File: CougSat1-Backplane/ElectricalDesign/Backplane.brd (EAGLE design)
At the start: 92 x 85 mm, 16 parts, among them J1 COUGSATBUSBACKPLANE, J2 COUGSATBUSBACKPLANE, J3 COUGSATBUSBACKPLANE, J4 COUGSATBUSBACKPLANE, J5 COUGSATBUSBACKPLANE, J6 COUGSATBUSBACKPLANE, J7 COUGSATBUSBACKPLANE, J8 COUGSATBUSBACKPLANE

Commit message: Updated Backplane Schematic
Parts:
- removed H3, H4: (no value), CougsInSpace:HOLE-3.3MM_PLAIN
- removed IMG1: COUGSINSPACELOGOSMALL, CougsInSpace:COUGSINSPACELOGO_SMALL
- removed IMG2: COUGSINSPACELOGOTEXT, CougsInSpace:COUGSINSPACETEXT
- removed IMG3: SIGNATUREHENDRIK, CougsInSpace:SIGNATURE_HENDRIK-MONOGRAM
- removed IMG4: SIGNATUREHENDRIK-HAM, CougsInSpace:SIGNATURE_HENDRIK-HAM
- added C1, C2: 100nF 10%, CougsInSpace-Capacitors:1608
- added J10, J9: Deployment Switch, CougsInSpace-Connectors:PICOLOCK1.5-04
- added R1, R2: 0Ω <20mΩ, CougsInSpace-Resistors:1608
- H1, H2: value (none) -> M3; device CougsInSpace:HOLE-3.3MM_PLAIN -> CougsInSpace-Hardware:MOUNTING_HOLE-3.3
- J1, J2, J3, J4, J5, J6, J7, J8: value COUGSATBUSBACKPLANE -> CougSat Socket; device CougsInSpace:COUGSATBUS_FEMALE-SODIMM -> CougsInSpace-Connectors:SODIMM-DDR1
- moved H2 75.1 mm to (14.0, 0.00)
- moved J1 62.6 mm to (0.00, -37.5)
- moved J2 62.6 mm to (0.00, -28.5)
- moved J3 62.6 mm to (0.00, -19.5)
- moved J4 62.6 mm to (0.00, -10.5)
- moved J5 62.6 mm to (0.00, 10.5)
- moved J6 62.6 mm to (0.00, 19.5)
- moved J7 62.6 mm to (0.00, 28.5)
- moved J8 62.6 mm to (0.00, 37.5)
- moved H1 17.3 mm to (-14.0, 0.00)
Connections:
- removed net COM_IRQ: J1.154, J1.156, J2.154, J2.156, J3.154, J3.156, J4.154, J4.156, J5.154, J5.156, J6.154, J6.156, J7.154, J7.156, J8.154, J8.156
- removed net COM_USART_CLK: J1.150, J1.152, J2.150, J2.152, J3.150, J3.152, J4.150, J4.152, J5.150, J5.152, J6.150, J6.152, J7.150, J7.152, J8.150, J8.152
- removed net COM_USART_RX: J1.146, J1.148, J2.146, J2.148, J3.146, J3.148, J4.146, J4.148, J5.146, J5.148, J6.146, J6.148, J7.146, J7.148, J8.146, J8.148
- removed net COM_USART_TX: J1.142, J1.144, J2.142, J2.144, J3.142, J3.144, J4.142, J4.144, J5.142, J5.144, J6.142, J6.144, J7.142, J7.144, J8.142, J8.144
- removed net CTRL_RESET: J1.174, J1.176, J2.174, J2.176, J3.174, J3.176, J4.174, J4.176, J5.174, J5.176, J6.174, J6.176, J7.174, J7.176, J8.174, J8.176
- removed net GPIO_153: J1.153, J2.153, J3.153, J4.153, J5.153, J6.153, J7.153, J8.153
- removed net GPIO_155: J1.155, J2.155, J3.155, J4.155, J5.155, J6.155, J7.155, J8.155
- removed net GPIO_157: J1.157, J2.157, J3.157, J4.157, J5.157, J6.157, J7.157, J8.157
- removed net GPIO_158: J1.158, J2.158, J3.158, J4.158, J5.158, J6.158, J7.158, J8.158
- removed net GPIO_159: J1.159, J2.159, J3.159, J4.159, J5.159, J6.159, J7.159, J8.159
- removed net GPIO_161: J1.161, J2.161, J3.161, J4.161, J5.161, J6.161, J7.161, J8.161
- removed net GPIO_163: J1.163, J2.163, J3.163, J4.163, J5.163, J6.163, J7.163, J8.163
- removed net GPIO_165: J1.165, J2.165, J3.165, J4.165, J5.165, J6.165, J7.165, J8.165
- removed net GPIO_167: J1.167, J2.167, J3.167, J4.167, J5.167, J6.167, J7.167, J8.167
- removed net PMIC_I2C_SCL: J1.183, J2.183, J3.183, J4.183, J5.183, J6.183, J7.183, J8.183
- removed net PMIC_I2C_SDA: J1.181, J2.181, J3.181, J4.181, J5.181, J6.181, J7.181, J8.181
- removed net PWR_CTRL_UMB: J1.170, J1.172, J2.170, J2.172, J3.170, J3.172, J4.170, J4.172, J5.170, J5.172, J6.170, J6.172, J7.170, J7.172, J8.170, J8.172
- removed net SUP_3V3_0: J1.10, J1.2, J1.4, J1.6, J1.8, J2.10, J2.2, J2.4, J2.6, J2.8, J3.10, J3.2, J3.4, J3.6, J3.8, J4.10, J4.2, J4.4, J4.6, J4.8, J5.10, J5.2, J5.4, J5.6, J5.8, J6.10, J6.2, J6.4, J6.6, J6.8, J7.10, J7.2, J7.4, J7.6, J7.8, J8.10, J8.2, J8.4, J8.6, J8.8
- removed net SUP_3V3_1: J1.12, J1.14, J1.16, J1.18, J1.20, J2.12, J2.14, J2.16, J2.18, J2.20, J3.12, J3.14, J3.16, J3.18, J3.20, J4.12, J4.14, J4.16, J4.18, J4.20, J5.12, J5.14, J5.16, J5.18, J5.20, J6.12, J6.14, J6.16, J6.18, J6.20, J7.12, J7.14, J7.16, J7.18, J7.20, J8.12, J8.14, J8.16, J8.18, J8.20
- removed net SUP_3V3_2: J1.21, J1.23, J1.25, J1.27, J1.29, J1.31, J1.33, J1.35, J1.37, J1.39, J2.21, J2.23, J2.25, J2.27, J2.29, J2.31, J2.33, J2.35, J2.37, J2.39, J3.21, J3.23, J3.25, J3.27, J3.29, J3.31, J3.33, J3.35, J3.37, J3.39, J4.21, J4.23, J4.25, J4.27, J4.29, J4.31, J4.33, J4.35, J4.37, J4.39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
- removed net SUP_3V3_3: J1.22, J1.24, J1.26, J1.28, J1.30, J1.32, J1.34, J1.36, J1.38, J1.40, J2.22, J2.24, J2.26, J2.28, J2.30, J2.32, J2.34, J2.36, J2.38, J2.40, J3.22, J3.24, J3.26, J3.28, J3.30, J3.32, J3.34, J3.36, J3.38, J3.40, J4.22, J4.24, J4.26, J4.28, J4.30, J4.32, J4.34, J4.36, J4.38, J4.40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
- removed net SUP_3V3_4: J1.42, J1.44, J1.46, J1.48, J1.50, J2.42, J2.44, J2.46, J2.48, J2.50, J3.42, J3.44, J3.46, J3.48, J3.50, J4.42, J4.44, J4.46, J4.48, J4.50, J5.42, J5.44, J5.46, J5.48, J5.50, J6.42, J6.44, J6.46, J6.48, J6.50, J7.42, J7.44, J7.46, J7.48, J7.50, J8.42, J8.44, J8.46, J8.48, J8.50
- removed net SUP_3V3_5: J1.52, J1.54, J1.56, J1.58, J1.60, J2.52, J2.54, J2.56, J2.58, J2.60, J3.52, J3.54, J3.56, J3.58, J3.60, J4.52, J4.54, J4.56, J4.58, J4.60, J5.52, J5.54, J5.56, J5.58, J5.60, J6.52, J6.54, J6.56, J6.58, J6.60, J7.52, J7.54, J7.56, J7.58, J7.60, J8.52, J8.54, J8.56, J8.58, J8.60
- removed net SUP_5V0_0: J1.62, J1.64, J1.66, J1.68, J1.70, J1.72, J1.74, J1.76, J1.78, J1.80, J2.62, J2.64, J2.66, J2.68, J2.70, J2.72, J2.74, J2.76, J2.78, J2.80, J3.62, J3.64, J3.66, J3.68, J3.70, J3.72, J3.74, J3.76, J3.78, J3.80, J4.62, J4.64, J4.66, J4.68, J4.70, J4.72, J4.74, J4.76, J4.78, J4.80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
- removed net SUP_5V0_1: J1.71, J1.73, J1.75, J1.77, J1.79, J1.81, J1.83, J1.85, J1.87, J1.89, J2.71, J2.73, J2.75, J2.77, J2.79, J2.81, J2.83, J2.85, J2.87, J2.89, J3.71, J3.73, J3.75, J3.77, J3.79, J3.81, J3.83, J3.85, J3.87, J3.89, J4.71, J4.73, J4.75, J4.77, J4.79, J4.81, J4.83, J4.85, J4.87, J4.89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
- removed net SUP_5VIN: J1.182, J1.184, J1.186, J1.188, J1.190, J1.192, J1.194, J1.196, J1.198, J1.200, J2.182, J2.184, J2.186, J2.188, J2.190, J2.192, J2.194, J2.196, J2.198, J2.200, J3.182, J3.184, J3.186, J3.188, J3.190, J3.192, J3.194, J3.196, J3.198, J3.200, J4.182, J4.184, J4.186, J4.188, J4.190, J4.192, J4.194, J4.196, J4.198, J4.200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
- removed net SUP_UNREG_0: J1.101, J1.103, J1.105, J1.107, J1.109, J1.91, J1.93, J1.95, J1.97, J1.99, J2.101, J2.103, J2.105, J2.107, J2.109, J2.91, J2.93, J2.95, J2.97, J2.99, J3.101, J3.103, J3.105, J3.107, J3.109, J3.91, J3.93, J3.95, J3.97, J3.99, J4.101, J4.103, J4.105, J4.107, J4.109, J4.91, J4.93, J4.95, J4.97, J4.99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
- removed net SUP_UNREG_1: J1.111, J1.113, J1.115, J1.117, J1.119, J1.121, J1.123, J1.125, J1.127, J1.129, J2.111, J2.113, J2.115, J2.117, J2.119, J2.121, J2.123, J2.125, J2.127, J2.129, J3.111, J3.113, J3.115, J3.117, J3.119, J3.121, J3.123, J3.125, J3.127, J3.129, J4.111, J4.113, J4.115, J4.117, J4.119, J4.121, J4.123, J4.125, J4.127, J4.129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
- new net BUS_JTAG_EN-0: J1.186, J1.188, J2.186, J2.188, J3.186, J3.188, J4.186, J4.188, J5.186, J5.188, J6.186, J6.188, J7.186, J7.188, J8.186, J8.188
- new net BUS_JTAG_EN-1: J1.190, J1.192, J2.190, J2.192, J3.190, J3.192, J4.190, J4.192, J5.190, J5.192, J6.190, J6.192, J7.190, J7.192, J8.190, J8.192
- new net BUS_JTAG_EN-2: J1.194, J1.196, J2.194, J2.196, J3.194, J3.196, J4.194, J4.196, J5.194, J5.196, J6.194, J6.196, J7.194, J7.196, J8.194, J8.196
- new net BUS_JTAG_EN-3: J1.198, J1.200, J2.198, J2.200, J3.198, J3.200, J4.198, J4.200, J5.198, J5.200, J6.198, J6.200, J7.198, J7.200, J8.198, J8.200
- new net CHASSIS: C1.1, C2.1, H1.1, H1.V1, H1.V2, H1.V3, H1.V4, H1.V5, H1.V6, H1.V7, H1.V8, H2.1, H2.V1, H2.V2, H2.V3, H2.V4, H2.V5, H2.V6, H2.V7, H2.V8, R1.2, R2.2
- new net COM_SPI_CS: J1.145, J1.147, J2.145, J2.147, J3.145, J3.147, J4.145, J4.147, J5.145, J5.147, J6.145, J6.147, J7.145, J7.147, J8.145, J8.147
- new net COM_SPI_MISO: J1.137, J1.139, J2.137, J2.139, J3.137, J3.139, J4.137, J4.139, J5.137, J5.139, J6.137, J6.139, J7.137, J7.139, J8.137, J8.139
- new net COM_SPI_MOSI: J1.141, J1.143, J2.141, J2.143, J3.141, J3.143, J4.141, J4.143, J5.141, J5.143, J6.141, J6.143, J7.141, J7.143, J8.141, J8.143
- new net COM_SPI_SCK: J1.133, J1.135, J2.133, J2.135, J3.133, J3.135, J4.133, J4.135, J5.133, J5.135, J6.133, J6.135, J7.133, J7.135, J8.133, J8.135
- new net CTRL_!RESET: J1.165, J1.167, J2.165, J2.167, J3.165, J3.167, J4.165, J4.167, J5.165, J5.167, J6.165, J6.167, J7.165, J7.167, J8.165, J8.167
- new net GPIO-0: J1.81, J1.83, J2.81, J2.83, J3.81, J3.83, J4.81, J4.83, J5.81, J5.83, J6.81, J6.83, J7.81, J7.83, J8.81, J8.83
- new net GPIO-1: J1.85, J1.87, J2.85, J2.87, J3.85, J3.87, J4.85, J4.87, J5.85, J5.87, J6.85, J6.87, J7.85, J7.87, J8.85, J8.87
- new net GPIO-2: J1.89, J1.91, J2.89, J2.91, J3.89, J3.91, J4.89, J4.91, J5.89, J5.91, J6.89, J6.91, J7.89, J7.91, J8.89, J8.91
- new net GPIO-3: J1.93, J1.95, J2.93, J2.95, J3.93, J3.95, J4.93, J4.95, J5.93, J5.95, J6.93, J6.95, J7.93, J7.95, J8.93, J8.95
- new net GPIO-4: J1.97, J1.99, J2.97, J2.99, J3.97, J3.99, J4.97, J4.99, J5.97, J5.99, J6.97, J6.99, J7.97, J7.99, J8.97, J8.99
- new net GPIO-5: J1.101, J1.103, J2.101, J2.103, J3.101, J3.103, J4.101, J4.103, J5.101, J5.103, J6.101, J6.103, J7.101, J7.103, J8.101, J8.103
- new net GPIO-6: J1.105, J1.107, J2.105, J2.107, J3.105, J3.107, J4.105, J4.107, J5.105, J5.107, J6.105, J6.107, J7.105, J7.107, J8.105, J8.107
- new net GPIO-7: J1.109, J1.111, J2.109, J2.111, J3.109, J3.111, J4.109, J4.111, J5.109, J5.111, J6.109, J6.111, J7.109, J7.111, J8.109, J8.111
- new net GPIO-8: J1.113, J1.115, J2.113, J2.115, J3.113, J3.115, J4.113, J4.115, J5.113, J5.115, J6.113, J6.115, J7.113, J7.115, J8.113, J8.115
- new net GPIO-9: J1.117, J1.119, J2.117, J2.119, J3.117, J3.119, J4.117, J4.119, J5.117, J5.119, J6.117, J6.119, J7.117, J7.119, J8.117, J8.119
- new net PR_3.3V-0: J1.1, J1.2, J1.3, J1.4, J2.1, J2.2, J2.3, J2.4, J3.1, J3.2, J3.3, J3.4, J4.1, J4.2, J4.3, J4.4, J5.1, J5.2, J5.3, J5.4, J6.1, J6.2, J6.3, J6.4, J7.1, J7.2, J7.3, J7.4, J8.1, J8.2, J8.3, J8.4
- new net PR_3.3V-1: J1.5, J1.6, J1.7, J1.8, J2.5, J2.6, J2.7, J2.8, J3.5, J3.6, J3.7, J3.8, J4.5, J4.6, J4.7, J4.8, J5.5, J5.6, J5.7, J5.8, J6.5, J6.6, J6.7, J6.8, J7.5, J7.6, J7.7, J7.8, J8.5, J8.6, J8.7, J8.8
- new net PR_3.3V-10: J1.41, J1.42, J1.43, J1.44, J2.41, J2.42, J2.43, J2.44, J3.41, J3.42, J3.43, J3.44, J4.41, J4.42, J4.43, J4.44, J5.41, J5.42, J5.43, J5.44, J6.41, J6.42, J6.43, J6.44, J7.41, J7.42, J7.43, J7.44, J8.41, J8.42, J8.43, J8.44
- new net PR_3.3V-11: J1.45, J1.46, J1.47, J1.48, J2.45, J2.46, J2.47, J2.48, J3.45, J3.46, J3.47, J3.48, J4.45, J4.46, J4.47, J4.48, J5.45, J5.46, J5.47, J5.48, J6.45, J6.46, J6.47, J6.48, J7.45, J7.46, J7.47, J7.48, J8.45, J8.46, J8.47, J8.48
- new net PR_3.3V-12: J1.49, J1.50, J1.51, J1.52, J2.49, J2.50, J2.51, J2.52, J3.49, J3.50, J3.51, J3.52, J4.49, J4.50, J4.51, J4.52, J5.49, J5.50, J5.51, J5.52, J6.49, J6.50, J6.51, J6.52, J7.49, J7.50, J7.51, J7.52, J8.49, J8.50, J8.51, J8.52
- new net PR_3.3V-2: J1.10, J1.11, J1.12, J1.9, J2.10, J2.11, J2.12, J2.9, J3.10, J3.11, J3.12, J3.9, J4.10, J4.11, J4.12, J4.9, J5.10, J5.11, J5.12, J5.9, J6.10, J6.11, J6.12, J6.9, J7.10, J7.11, J7.12, J7.9, J8.10, J8.11, J8.12, J8.9
- new net PR_3.3V-3: J1.13, J1.14, J1.15, J1.16, J2.13, J2.14, J2.15, J2.16, J3.13, J3.14, J3.15, J3.16, J4.13, J4.14, J4.15, J4.16, J5.13, J5.14, J5.15, J5.16, J6.13, J6.14, J6.15, J6.16, J7.13, J7.14, J7.15, J7.16, J8.13, J8.14, J8.15, J8.16
- new net PR_3.3V-4: J1.17, J1.18, J1.19, J1.20, J2.17, J2.18, J2.19, J2.20, J3.17, J3.18, J3.19, J3.20, J4.17, J4.18, J4.19, J4.20, J5.17, J5.18, J5.19, J5.20, J6.17, J6.18, J6.19, J6.20, J7.17, J7.18, J7.19, J7.20, J8.17, J8.18, J8.19, J8.20
- new net PR_3.3V-5: J1.21, J1.22, J1.23, J1.24, J2.21, J2.22, J2.23, J2.24, J3.21, J3.22, J3.23, J3.24, J4.21, J4.22, J4.23, J4.24, J5.21, J5.22, J5.23, J5.24, J6.21, J6.22, J6.23, J6.24, J7.21, J7.22, J7.23, J7.24, J8.21, J8.22, J8.23, J8.24
- new net PR_3.3V-6: J1.25, J1.26, J1.27, J1.28, J2.25, J2.26, J2.27, J2.28, J3.25, J3.26, J3.27, J3.28, J4.25, J4.26, J4.27, J4.28, J5.25, J5.26, J5.27, J5.28, J6.25, J6.26, J6.27, J6.28, J7.25, J7.26, J7.27, J7.28, J8.25, J8.26, J8.27, J8.28
- new net PR_3.3V-7: J1.29, J1.30, J1.31, J1.32, J2.29, J2.30, J2.31, J2.32, J3.29, J3.30, J3.31, J3.32, J4.29, J4.30, J4.31, J4.32, J5.29, J5.30, J5.31, J5.32, J6.29, J6.30, J6.31, J6.32, J7.29, J7.30, J7.31, J7.32, J8.29, J8.30, J8.31, J8.32
- new net PR_3.3V-8: J1.33, J1.34, J1.35, J1.36, J2.33, J2.34, J2.35, J2.36, J3.33, J3.34, J3.35, J3.36, J4.33, J4.34, J4.35, J4.36, J5.33, J5.34, J5.35, J5.36, J6.33, J6.34, J6.35, J6.36, J7.33, J7.34, J7.35, J7.36, J8.33, J8.34, J8.35, J8.36
- new net PR_3.3V-9: J1.37, J1.38, J1.39, J1.40, J2.37, J2.38, J2.39, J2.40, J3.37, J3.38, J3.39, J3.40, J4.37, J4.38, J4.39, J4.40, J5.37, J5.38, J5.39, J5.40, J6.37, J6.38, J6.39, J6.40, J7.37, J7.38, J7.39, J7.40, J8.37, J8.38, J8.39, J8.40
- new net PR_BATT-0: J1.53, J1.54, J1.55, J1.56, J2.53, J2.54, J2.55, J2.56, J3.53, J3.54, J3.55, J3.56, J4.53, J4.54, J4.55, J4.56, J5.53, J5.54, J5.55, J5.56, J6.53, J6.54, J6.55, J6.56, J7.53, J7.54, J7.55, J7.56, J8.53, J8.54, J8.55, J8.56
- new net PR_BATT-1: J1.57, J1.58, J1.59, J1.60, J2.57, J2.58, J2.59, J2.60, J3.57, J3.58, J3.59, J3.60, J4.57, J4.58, J4.59, J4.60, J5.57, J5.58, J5.59, J5.60, J6.57, J6.58, J6.59, J6.60, J7.57, J7.58, J7.59, J7.60, J8.57, J8.58, J8.59, J8.60
- new net PR_BATT-2: J1.61, J1.62, J1.63, J1.64, J2.61, J2.62, J2.63, J2.64, J3.61, J3.62, J3.63, J3.64, J4.61, J4.62, J4.63, J4.64, J5.61, J5.62, J5.63, J5.64, J6.61, J6.62, J6.63, J6.64, J7.61, J7.62, J7.63, J7.64, J8.61, J8.62, J8.63, J8.64
- new net PR_BATT-3: J1.65, J1.66, J1.67, J1.68, J2.65, J2.66, J2.67, J2.68, J3.65, J3.66, J3.67, J3.68, J4.65, J4.66, J4.67, J4.68, J5.65, J5.66, J5.67, J5.68, J6.65, J6.66, J6.67, J6.68, J7.65, J7.66, J7.67, J7.68, J8.65, J8.66, J8.67, J8.68
- new net PR_BATT-4: J1.69, J1.70, J1.71, J1.72, J2.69, J2.70, J2.71, J2.72, J3.69, J3.70, J3.71, J3.72, J4.69, J4.70, J4.71, J4.72, J5.69, J5.70, J5.71, J5.72, J6.69, J6.70, J6.71, J6.72, J7.69, J7.70, J7.71, J7.72, J8.69, J8.70, J8.71, J8.72
- new net PR_BATT-5: J1.73, J1.74, J1.75, J1.76, J2.73, J2.74, J2.75, J2.76, J3.73, J3.74, J3.75, J3.76, J4.73, J4.74, J4.75, J4.76, J5.73, J5.74, J5.75, J5.76, J6.73, J6.74, J6.75, J6.76, J7.73, J7.74, J7.75, J7.76, J8.73, J8.74, J8.75, J8.76
- new net PR_BATT-6: J1.77, J1.78, J1.79, J1.80, J2.77, J2.78, J2.79, J2.80, J3.77, J3.78, J3.79, J3.80, J4.77, J4.78, J4.79, J4.80, J5.77, J5.78, J5.79, J5.80, J6.77, J6.78, J6.79, J6.80, J7.77, J7.78, J7.79, J7.80, J8.77, J8.78, J8.79, J8.80
- net BUS_I2C0_IRQ: now also J1.181, J1.183, J2.181, J2.183, J3.181, J3.183, J4.181, J4.183, J5.181, J5.183, J6.181, J6.183, J7.181, J7.183, J8.181, J8.183; no longer J1.177, J1.179, J2.177, J2.179, J3.177, J3.179, J4.177, J4.179, J5.177, J5.179, J6.177, J6.179, J7.177, J7.179, J8.177, J8.179
- net BUS_I2C0_SCL: now also J1.177, J1.179, J2.177, J2.179, J3.177, J3.179, J4.177, J4.179, J5.177, J5.179, J6.177, J6.179, J7.177, J7.179, J8.177, J8.179; no longer J1.173, J1.175, J2.173, J2.175, J3.173, J3.175, J4.173, J4.175, J5.173, J5.175, J6.173, J6.175, J7.173, J7.175, J8.173, J8.175
- net BUS_I2C0_SDA: now also J1.173, J1.175, J2.173, J2.175, J3.173, J3.175, J4.173, J4.175, J5.173, J5.175, J6.173, J6.175, J7.173, J7.175, J8.173, J8.175; no longer J1.169, J1.171, J2.169, J2.171, J3.169, J3.171, J4.169, J4.171, J5.169, J5.171, J6.169, J6.171, J7.169, J7.171, J8.169, J8.171
- net BUS_I2C1_IRQ: now also J1.129, J1.131, J2.129, J2.131, J3.129, J3.131, J4.129, J4.131, J5.129, J5.131, J6.129, J6.131, J7.129, J7.131, J8.129, J8.131; no longer J1.164, J2.164, J3.164, J4.164, J5.164, J6.164, J7.164, J8.164
- net BUS_I2C1_SCL: now also J1.125, J1.127, J2.125, J2.127, J3.125, J3.127, J4.125, J4.127, J5.125, J5.127, J6.125, J6.127, J7.125, J7.127, J8.125, J8.127; no longer J1.160, J2.160, J3.160, J4.160, J5.160, J6.160, J7.160, J8.160
- net BUS_I2C1_SDA: now also J1.121, J1.123, J2.121, J2.123, J3.121, J3.123, J4.121, J4.123, J5.121, J5.123, J6.121, J6.123, J7.121, J7.123, J8.121, J8.123; no longer J1.162, J2.162, J3.162, J4.162, J5.162, J6.162, J7.162, J8.162
- net BUS_SPI_MISO: now also J1.153, J1.155, J2.153, J2.155, J3.153, J3.155, J4.153, J4.155, J5.153, J5.155, J6.153, J6.155, J7.153, J7.155, J8.153, J8.155; no longer J1.145, J1.147, J2.145, J2.147, J3.145, J3.147, J4.145, J4.147, J5.145, J5.147, J6.145, J6.147, J7.145, J7.147, J8.145, J8.147
- net BUS_SPI_MOSI: now also J1.157, J1.159, J2.157, J2.159, J3.157, J3.159, J4.157, J4.159, J5.157, J5.159, J6.157, J6.159, J7.157, J7.159, J8.157, J8.159; no longer J1.149, J1.151, J2.149, J2.151, J3.149, J3.151, J4.149, J4.151, J5.149, J5.151, J6.149, J6.151, J7.149, J7.151, J8.149, J8.151
- net BUS_SPI_SCK: now also J1.149, J1.151, J2.149, J2.151, J3.149, J3.151, J4.149, J4.151, J5.149, J5.151, J6.149, J6.151, J7.149, J7.151, J8.149, J8.151; no longer J1.141, J1.143, J2.141, J2.143, J3.141, J3.143, J4.141, J4.143, J5.141, J5.143, J6.141, J6.143, J7.141, J7.143, J8.141, J8.143
- net CTRL_SYNC: now also J1.169, J1.171, J2.169, J2.171, J3.169, J3.171, J4.169, J4.171, J5.169, J5.171, J6.169, J6.171, J7.169, J7.171, J8.169, J8.171; no longer J1.178, J1.180, J2.178, J2.180, J3.178, J3.180, J4.178, J4.180, J5.178, J5.180, J6.178, J6.180, J7.178, J7.180, J8.178, J8.180
- net PGND: now also C1.2, C2.2, J1.142, J1.144, J1.146, J1.148, J1.150, J1.152, J1.154, J1.156, J1.158, J1.160, J1.162, J1.164, J1.166, J1.168, J1.170, J1.172, J1.174, J1.176, J1.178, J1.180, J1.182, J1.184, J10.3, J10.4, J2.142, J2.144, J2.146, J2.148, J2.150, J2.152, J2.154, J2.156, J2.158, J2.160, J2.162, J2.164, J2.166, J2.168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; no longer J1.1, J1.11, J1.13, J1.131, J1.133, J1.135, J1.137, J1.139, J1.15, J1.17, J1.19, J1.3, J1.41, J1.43, J1.45, J1.47, J1.49, J1.5, J1.51, J1.53, J1.55, J1.57, J1.59, J1.61, J1.63, J1.65, J1.67, J1.69, J1.7, J1.9, J2.1, J2.11, J2.13, J2.131, J2.133, J2.135, J2.137, J2.139, J2.15, J2.17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
- net PWR_CTRL_SW: now also J1.161, J1.163, J10.1, J10.2, J2.161, J2.163, J3.161, J3.163, J4.161, J4.163, J5.161, J5.163, J6.161, J6.163, J7.161, J7.163, J8.161, J8.163, J9.1, J9.2; no longer J1.166, J1.168, J2.166, J2.168, J3.166, J3.168, J4.166, J4.168, J5.166, J5.168, J6.166, J6.168, J7.166, J7.168, J8.166, J8.168
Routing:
- net CTRL_SYNC: track 135.0 -> 0.00 mm, vias 8 -> 0
- net CTRL_RESET: track 134.7 -> 0.00 mm, vias 8 -> 0
- net PWR_CTRL_UMB: track 133.1 -> 0.00 mm, vias 8 -> 0
- net GPIO_155: track 129.9 -> 0.00 mm, vias 8 -> 0
- net BUS_SPI_MISO: track 129.4 -> 0.00 mm, vias 8 -> 0
- net SUP_5VIN: track 128.2 -> 0.00 mm, vias 8 -> 0
- net GPIO_157: track 124.9 -> 0.00 mm, vias 8 -> 0
- net GPIO_153: track 124.8 -> 0.00 mm, vias 8 -> 0
- net GPIO_159: track 122.4 -> 0.00 mm, vias 8 -> 0
- net BUS_SPI_MOSI: track 120.5 -> 0.00 mm, vias 8 -> 0
- net BUS_JTAG_TCK: track 119.0 -> 0.00 mm, vias 8 -> 0
- net BUS_SPI_SCK: track 118.3 -> 0.00 mm, vias 8 -> 0
- net BUS_I2C0_IRQ: track 115.7 -> 0.00 mm, vias 8 -> 0
- net PMIC_I2C_SDA: track 114.7 -> 0.00 mm, vias 8 -> 0
- net PWR_CTRL_SW: track 114.3 -> 0.00 mm, vias 8 -> 0
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- removed copper zone on layer 1, net PGND
- removed copper zone on layer 1, net SUP_3V3_0
- removed copper zone on layer 1, net SUP_3V3_1
- removed copper zone on layer 1, net SUP_3V3_2
- removed copper zone on layer 1, net SUP_3V3_3
- removed copper zone on layer 1, net SUP_3V3_4
- removed copper zone on layer 1, net SUP_3V3_5
- removed copper zone on layer 1, net SUP_5V0_0
- removed copper zone on layer 1, net SUP_5V0_1
- removed copper zone on layer 1, net SUP_UNREG_0
- removed copper zone on layer 1, net SUP_UNREG_1
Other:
- board size 92 x 85 mm -> 82.8 x 86 mm
- board text removed: "Backplane V2.1.0 1813"

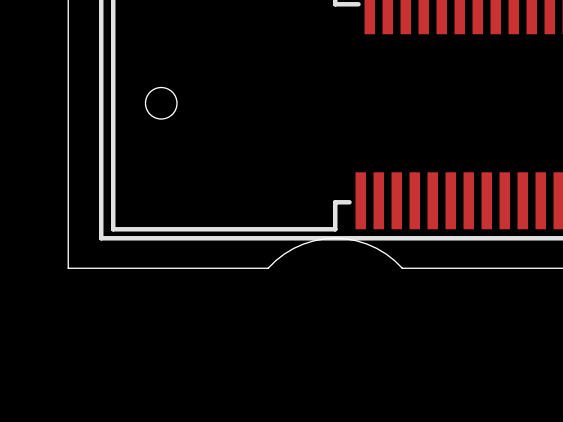
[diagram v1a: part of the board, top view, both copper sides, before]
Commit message: Wrote Backplane Design Document
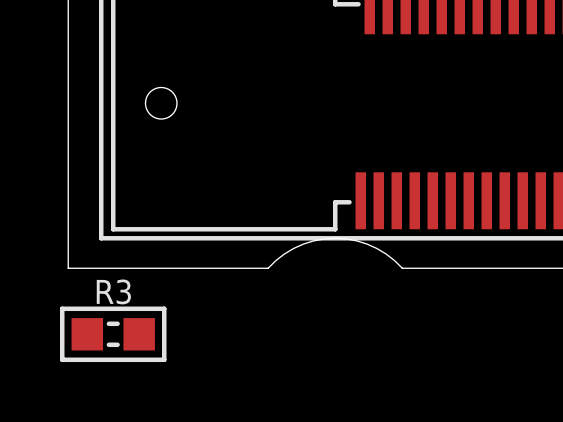
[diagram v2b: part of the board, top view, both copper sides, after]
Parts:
- added R3: 0Ω <20mΩ, CougsInSpace-Resistors:1608
- J10, J9: value Deployment Switch -> Separation Switch
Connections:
- net CHASSIS: now also R3.2
- net PGND: now also R3.1

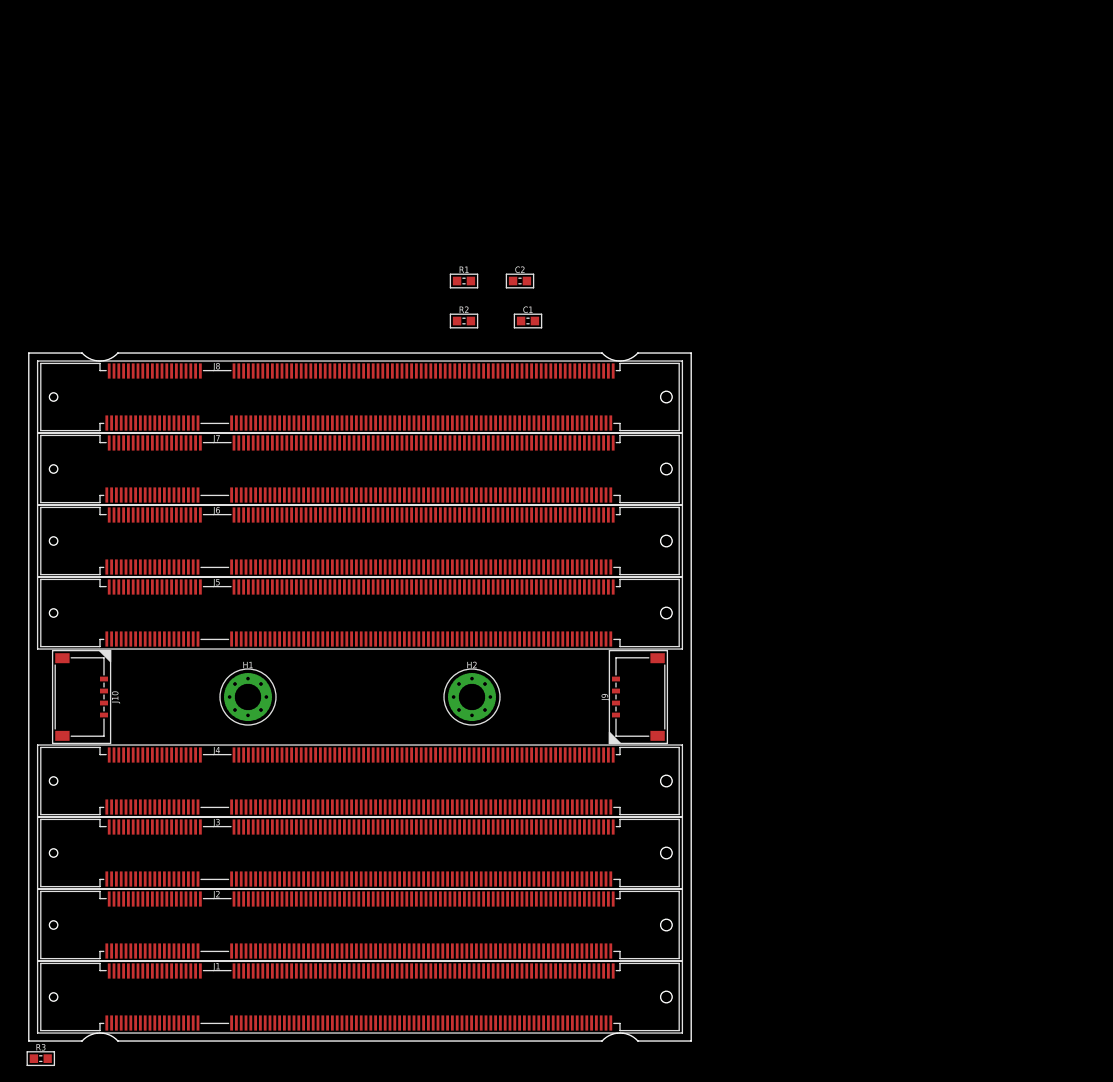
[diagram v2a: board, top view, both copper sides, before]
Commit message: Laid Out Backplane
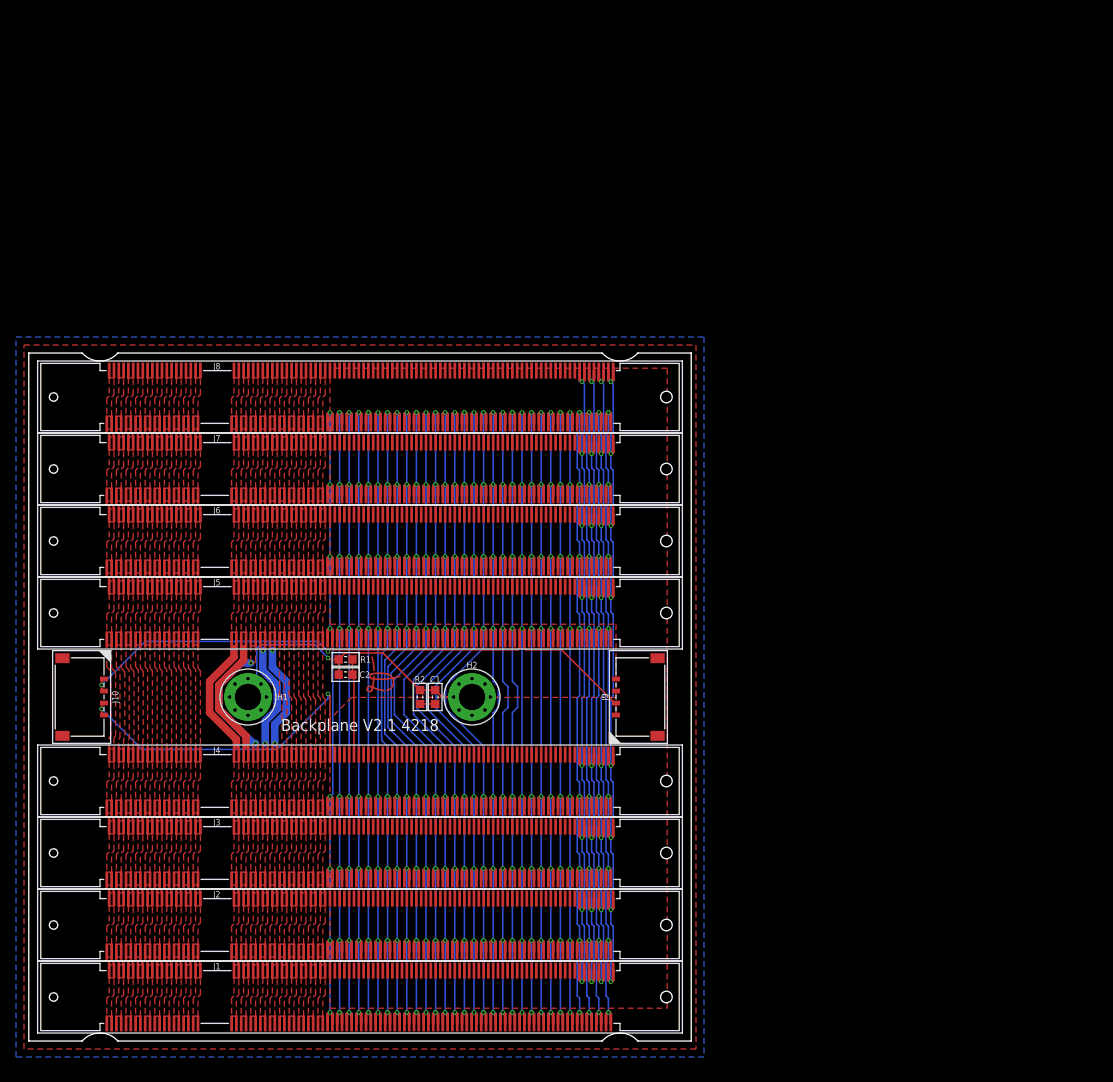
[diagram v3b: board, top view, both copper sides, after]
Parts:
- removed R3: 0Ω <20mΩ, CougsInSpace-Resistors:1608
- added LOGO1: SIGNATUREBRADLEY, CougsInSpace-Aesthetics:SIGN-BRADLEY
- moved C2 53.8 mm to (-1.80, 2.80)
- moved R1 49.6 mm to (-1.80, 4.70), turned to 180 degrees
- moved C1 48.4 mm to (9.40, 0.00), turned to 270 degrees
- moved R2 47.3 mm to (7.50, 0.00), turned to 90 degrees
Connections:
- net CHASSIS: no longer R3.2
- net PGND: no longer R3.1
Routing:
- net PWR_CTRL_SW: track 0.00 -> 173.9 mm, vias 0 -> 10
- net COM_SPI_MOSI: track 0.00 -> 102.9 mm, vias 0 -> 8
- net COM_SPI_MISO: track 0.00 -> 102.9 mm, vias 0 -> 8
- net COM_SPI_SCK: track 0.00 -> 102.9 mm, vias 0 -> 8
- net COM_SPI_CS: track 0.00 -> 102.9 mm, vias 0 -> 8
- net BUS_I2C1_SDA: track 0.00 -> 102.3 mm, vias 0 -> 8
- net BUS_I2C1_SCL: track 0.00 -> 102.3 mm, vias 0 -> 8
- net BUS_I2C1_IRQ: track 0.00 -> 102.3 mm, vias 0 -> 8
- net GPIO-9: track 0.00 -> 101.6 mm, vias 0 -> 8
- net GPIO-8: track 0.00 -> 100.9 mm, vias 0 -> 8
- net BUS_JTAG_EN-0: track 0.00 -> 100.7 mm, vias 0 -> 8
- net BUS_JTAG_EN-2: track 0.00 -> 100.7 mm, vias 0 -> 8
- net BUS_JTAG_EN-1: track 0.00 -> 100.7 mm, vias 0 -> 8
- net BUS_JTAG_TMS: track 0.00 -> 100.7 mm, vias 0 -> 8
- net BUS_JTAG_TCK: track 0.00 -> 100.7 mm, vias 0 -> 8
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- added copper zone on layer 16, net BALANCING-BOTTOM
- added copper zone on layer 1, net BALANCING-TOP
- added copper zone on layer 1, net BUS_I2C0_IRQ
- added copper zone on layer 1, net BUS_I2C0_SCL
- added copper zone on layer 1, net BUS_I2C0_SDA
- added copper zone on layer 1, net BUS_I2C1_IRQ
- added copper zone on layer 1, net BUS_I2C1_SCL
- added copper zone on layer 1, net BUS_I2C1_SDA
- added copper zone on layer 1, net BUS_JTAG_EN-0
- added copper zone on layer 1, net BUS_JTAG_EN-1
- added copper zone on layer 1, net BUS_JTAG_EN-2
- added copper zone on layer 1, net BUS_JTAG_EN-3
- added copper zone on layer 1, net BUS_JTAG_TCK
- added copper zone on layer 1, net BUS_JTAG_TDI
- added copper zone on layer 1, net BUS_JTAG_TDO
- added copper zone on layer 1, net BUS_JTAG_TMS
- added copper zone on layer 1, net BUS_SPI_MISO
- added copper zone on layer 1, net BUS_SPI_MOSI
- added copper zone on layer 1, net BUS_SPI_SCK
- added copper zone on layer 1, net COM_SPI_CS
- added copper zone on layer 1, net COM_SPI_MISO
- added copper zone on layer 1, net COM_SPI_MOSI
- added copper zone on layer 1, net COM_SPI_SCK
- added copper zone on layer 1, net CTRL_!RESET
- added copper zone on layer 1, net CTRL_SYNC
- added copper zone on layer 1, net GPIO-0
- added copper zone on layer 1, net GPIO-1
- added copper zone on layer 1, net GPIO-2
- added copper zone on layer 1, net GPIO-3
- added copper zone on layer 1, net GPIO-4
- added copper zone on layer 1, net GPIO-5
- added copper zone on layer 1, net GPIO-6
- added copper zone on layer 1, net GPIO-7
- added copper zone on layer 1, net GPIO-8
- added copper zone on layer 1, net GPIO-9
- added copper zone on layer 1, net PGND
- added copper zone on layer 1, net PR_3.3V-0
- added copper zone on layer 1, net PR_3.3V-1
- added copper zone on layer 1, net PR_3.3V-10
- added copper zone on layer 1, net PR_3.3V-11
- added copper zone on layer 1, net PR_3.3V-12
- added copper zone on layer 1, net PR_3.3V-2
- added copper zone on layer 1, net PR_3.3V-3
- added copper zone on layer 1, net PR_3.3V-4
- added copper zone on layer 1, net PR_3.3V-5
- added copper zone on layer 1, net PR_3.3V-6
- added copper zone on layer 1, net PR_3.3V-7
- added copper zone on layer 1, net PR_3.3V-8
- added copper zone on layer 1, net PR_3.3V-9
- added copper zone on layer 1, net PR_BATT-0
- added copper zone on layer 1, net PR_BATT-1
- added copper zone on layer 1, net PR_BATT-2
- added copper zone on layer 1, net PR_BATT-3
- added copper zone on layer 1, net PR_BATT-4
- added copper zone on layer 1, net PR_BATT-5
- added copper zone on layer 1, net PR_BATT-6
- added copper zone on layer 1, net PWR_CTRL_SW
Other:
- board text added: "Backplane V2.1 4218"

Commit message: Generate Gerbers
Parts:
- J10, J9: value Separation Switch -> CougSat Socket; device CougsInSpace-Connectors:PICOLOCK1.5-04 -> CougsInSpace-Connectors:SODIMM-DDR1
- J5, J6: value CougSat Socket -> Separation Switch; device CougsInSpace-Connectors:SODIMM-DDR1 -> CougsInSpace-Connectors:PICOLOCK1.5-04
- moved J10 49.3 mm to (0.00, 37.5), turned to 0 degrees
- moved J9 42.9 mm to (0.00, 28.5), turned to 0 degrees
- moved J6 37.5 mm to (32.0, 0.00), turned to 270 degrees
- moved J5 33.7 mm to (-32.0, 0.00), turned to 90 degrees
- moved J7 18.0 mm to (0.00, 10.5)
- moved J8 18.0 mm to (0.00, 19.5)
- moved R1 10.4 mm to (7.50, 0.00), turned to 90 degrees
- moved R2 10.4 mm to (-1.80, 4.70), turned to 180 degrees
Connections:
- net BUS_I2C0_IRQ: now also J10.181, J10.183, J9.181, J9.183; no longer J5.181, J5.183, J6.181, J6.183
- net BUS_I2C0_SCL: now also J10.177, J10.179, J9.177, J9.179; no longer J5.177, J5.179, J6.177, J6.179
- net BUS_I2C0_SDA: now also J10.173, J10.175, J9.173, J9.175; no longer J5.173, J5.175, J6.173, J6.175
- net BUS_I2C1_IRQ: now also J10.129, J10.131, J9.129, J9.131; no longer J5.129, J5.131, J6.129, J6.131
- net BUS_I2C1_SCL: now also J10.125, J10.127, J9.125, J9.127; no longer J5.125, J5.127, J6.125, J6.127
- net BUS_I2C1_SDA: now also J10.121, J10.123, J9.121, J9.123; no longer J5.121, J5.123, J6.121, J6.123
- net BUS_JTAG_EN-0: now also J10.186, J10.188, J9.186, J9.188; no longer J5.186, J5.188, J6.186, J6.188
- net BUS_JTAG_EN-1: now also J10.190, J10.192, J9.190, J9.192; no longer J5.190, J5.192, J6.190, J6.192
- net BUS_JTAG_EN-2: now also J10.194, J10.196, J9.194, J9.196; no longer J5.194, J5.196, J6.194, J6.196
- net BUS_JTAG_EN-3: now also J10.198, J10.200, J9.198, J9.200; no longer J5.198, J5.200, J6.198, J6.200
- net BUS_JTAG_TCK: now also J10.185, J10.187, J9.185, J9.187; no longer J5.185, J5.187, J6.185, J6.187
- net BUS_JTAG_TDI: now also J10.189, J10.191, J9.189, J9.191; no longer J5.189, J5.191, J6.189, J6.191
- net BUS_JTAG_TDO: now also J10.193, J10.195, J9.193, J9.195; no longer J5.193, J5.195, J6.193, J6.195
- net BUS_JTAG_TMS: now also J10.197, J10.199, J9.197, J9.199; no longer J5.197, J5.199, J6.197, J6.199
- net BUS_SPI_MISO: now also J10.153, J10.155, J9.153, J9.155; no longer J5.153, J5.155, J6.153, J6.155
- net BUS_SPI_MOSI: now also J10.157, J10.159, J9.157, J9.159; no longer J5.157, J5.159, J6.157, J6.159
- net BUS_SPI_SCK: now also J10.149, J10.151, J9.149, J9.151; no longer J5.149, J5.151, J6.149, J6.151
- net COM_SPI_CS: now also J10.145, J10.147, J9.145, J9.147; no longer J5.145, J5.147, J6.145, J6.147
- net COM_SPI_MISO: now also J10.137, J10.139, J9.137, J9.139; no longer J5.137, J5.139, J6.137, J6.139
- net COM_SPI_MOSI: now also J10.141, J10.143, J9.141, J9.143; no longer J5.141, J5.143, J6.141, J6.143
- net COM_SPI_SCK: now also J10.133, J10.135, J9.133, J9.135; no longer J5.133, J5.135, J6.133, J6.135
- net CTRL_!RESET: now also J10.165, J10.167, J9.165, J9.167; no longer J5.165, J5.167, J6.165, J6.167
- net CTRL_SYNC: now also J10.169, J10.171, J9.169, J9.171; no longer J5.169, J5.171, J6.169, J6.171
- net GPIO-0: now also J10.81, J10.83, J9.81, J9.83; no longer J5.81, J5.83, J6.81, J6.83
- net GPIO-1: now also J10.85, J10.87, J9.85, J9.87; no longer J5.85, J5.87, J6.85, J6.87
- net GPIO-2: now also J10.89, J10.91, J9.89, J9.91; no longer J5.89, J5.91, J6.89, J6.91
- net GPIO-3: now also J10.93, J10.95, J9.93, J9.95; no longer J5.93, J5.95, J6.93, J6.95
- net GPIO-4: now also J10.97, J10.99, J9.97, J9.99; no longer J5.97, J5.99, J6.97, J6.99
- net GPIO-5: now also J10.101, J10.103, J9.101, J9.103; no longer J5.101, J5.103, J6.101, J6.103
- net GPIO-6: now also J10.105, J10.107, J9.105, J9.107; no longer J5.105, J5.107, J6.105, J6.107
- net GPIO-7: now also J10.109, J10.111, J9.109, J9.111; no longer J5.109, J5.111, J6.109, J6.111
- net GPIO-8: now also J10.113, J10.115, J9.113, J9.115; no longer J5.113, J5.115, J6.113, J6.115
- net GPIO-9: now also J10.117, J10.119, J9.117, J9.119; no longer J5.117, J5.119, J6.117, J6.119
- net PGND: now also J10.100, J10.102, J10.104, J10.106, J10.108, J10.110, J10.112, J10.114, J10.116, J10.118, J10.120, J10.122, J10.124, J10.126, J10.128, J10.130, J10.132, J10.134, J10.136, J10.138, J10.140, J10.142, J10.144, J10.146, J10.148, J10.150, J10.152, J10.154, J10.156, J10.158, J10.160, J10.162, J10.164, J10.166, J10.168, J10.170, J10.172, J10.174, J10.176, J10.178, J10.180, J10.182, J10.184, J10.82, J10.84, J10.86, J10.88, J10.90, J10.92, J10.94, J10.96, J10.98, J5.3, J5.4, J6.3, J6.4, J9.100, J9.102, J9.104, J9.106, J9.108, J9.110, J9.112, J9.114, J9.116, J9.118, J9.120, J9.122, J9.124, J9.126, J9.128, J9.130, J9.132, J9.134, J9.136, J9.138, J9.140, J9.142, J9.144, J9.146, J9.148, J9.150, J9.152, J9.154, J9.156, J9.158, J9.160, J9.162, J9.164, J9.166, J9.168, J9.170, J9.172, J9.174, J9.176, J9.178, J9.180, J9.182, J9.184, J9.82, J9.84, J9.86, J9.88, J9.90, J9.92, J9.94, J9.96, J9.98; no longer J10.3, J10.4, J5.100, J5.102, J5.104, J5.106, J5.108, J5.110, J5.112, J5.114, J5.116, J5.118, J5.120, J5.122, J5.124, J5.126, J5.128, J5.130, J5.132, J5.134, J5.136, J5.138, J5.140, J5.142, J5.144, J5.146, J5.148, J5.150, J5.152, J5.154, J5.156, J5.158, J5.160, J5.162, J5.164, J5.166, J5.168, J5.170, J5.172, J5.174, J5.176, J5.178, J5.180, J5.182, J5.184, J5.82, J5.84, J5.86, J5.88, J5.90, J5.92, J5.94, J5.96, J5.98, J6.100, J6.102, J6.104, J6.106, J6.108, J6.110, J6.112, J6.114, J6.116, J6.118, J6.120, J6.122, J6.124, J6.126, J6.128, J6.130, J6.132, J6.134, J6.136, J6.138, J6.140, J6.142, J6.144, J6.146, J6.148, J6.150, J6.152, J6.154, J6.156, J6.158, J6.160, J6.162, J6.164, J6.166, J6.168, J6.170, J6.172, J6.174, J6.176, J6.178, J6.180, J6.182, J6.184, J6.82, J6.84, J6.86, J6.88, J6.90, J6.92, J6.94, J6.96, J6.98, J9.3, J9.4
- net PR_3.3V-0: now also J10.1, J10.2, J10.3, J10.4, J9.1, J9.2, J9.3, J9.4; no longer J5.1, J5.2, J5.3, J5.4, J6.1, J6.2, J6.3, J6.4
- net PR_3.3V-1: now also J10.5, J10.6, J10.7, J10.8, J9.5, J9.6, J9.7, J9.8; no longer J5.5, J5.6, J5.7, J5.8, J6.5, J6.6, J6.7, J6.8
- net PR_3.3V-10: now also J10.41, J10.42, J10.43, J10.44, J9.41, J9.42, J9.43, J9.44; no longer J5.41, J5.42, J5.43, J5.44, J6.41, J6.42, J6.43, J6.44
- net PR_3.3V-11: now also J10.45, J10.46, J10.47, J10.48, J9.45, J9.46, J9.47, J9.48; no longer J5.45, J5.46, J5.47, J5.48, J6.45, J6.46, J6.47, J6.48
- net PR_3.3V-12: now also J10.49, J10.50, J10.51, J10.52, J9.49, J9.50, J9.51, J9.52; no longer J5.49, J5.50, J5.51, J5.52, J6.49, J6.50, J6.51, J6.52
- net PR_3.3V-2: now also J10.10, J10.11, J10.12, J10.9, J9.10, J9.11, J9.12, J9.9; no longer J5.10, J5.11, J5.12, J5.9, J6.10, J6.11, J6.12, J6.9
- net PR_3.3V-3: now also J10.13, J10.14, J10.15, J10.16, J9.13, J9.14, J9.15, J9.16; no longer J5.13, J5.14, J5.15, J5.16, J6.13, J6.14, J6.15, J6.16
- net PR_3.3V-4: now also J10.17, J10.18, J10.19, J10.20, J9.17, J9.18, J9.19, J9.20; no longer J5.17, J5.18, J5.19, J5.20, J6.17, J6.18, J6.19, J6.20
- net PR_3.3V-5: now also J10.21, J10.22, J10.23, J10.24, J9.21, J9.22, J9.23, J9.24; no longer J5.21, J5.22, J5.23, J5.24, J6.21, J6.22, J6.23, J6.24
- net PR_3.3V-6: now also J10.25, J10.26, J10.27, J10.28, J9.25, J9.26, J9.27, J9.28; no longer J5.25, J5.26, J5.27, J5.28, J6.25, J6.26, J6.27, J6.28
- net PR_3.3V-7: now also J10.29, J10.30, J10.31, J10.32, J9.29, J9.30, J9.31, J9.32; no longer J5.29, J5.30, J5.31, J5.32, J6.29, J6.30, J6.31, J6.32
- net PR_3.3V-8: now also J10.33, J10.34, J10.35, J10.36, J9.33, J9.34, J9.35, J9.36; no longer J5.33, J5.34, J5.35, J5.36, J6.33, J6.34, J6.35, J6.36
- net PR_3.3V-9: now also J10.37, J10.38, J10.39, J10.40, J9.37, J9.38, J9.39, J9.40; no longer J5.37, J5.38, J5.39, J5.40, J6.37, J6.38, J6.39, J6.40
- net PR_BATT-0: now also J10.53, J10.54, J10.55, J10.56, J9.53, J9.54, J9.55, J9.56; no longer J5.53, J5.54, J5.55, J5.56, J6.53, J6.54, J6.55, J6.56
- net PR_BATT-1: now also J10.57, J10.58, J10.59, J10.60, J9.57, J9.58, J9.59, J9.60; no longer J5.57, J5.58, J5.59, J5.60, J6.57, J6.58, J6.59, J6.60
- net PR_BATT-2: now also J10.61, J10.62, J10.63, J10.64, J9.61, J9.62, J9.63, J9.64; no longer J5.61, J5.62, J5.63, J5.64, J6.61, J6.62, J6.63, J6.64
- net PR_BATT-3: now also J10.65, J10.66, J10.67, J10.68, J9.65, J9.66, J9.67, J9.68; no longer J5.65, J5.66, J5.67, J5.68, J6.65, J6.66, J6.67, J6.68
- net PR_BATT-4: now also J10.69, J10.70, J10.71, J10.72, J9.69, J9.70, J9.71, J9.72; no longer J5.69, J5.70, J5.71, J5.72, J6.69, J6.70, J6.71, J6.72
- net PR_BATT-5: now also J10.73, J10.74, J10.75, J10.76, J9.73, J9.74, J9.75, J9.76; no longer J5.73, J5.74, J5.75, J5.76, J6.73, J6.74, J6.75, J6.76
- net PR_BATT-6: now also J10.77, J10.78, J10.79, J10.80, J9.77, J9.78, J9.79, J9.80; no longer J5.77, J5.78, J5.79, J5.80, J6.77, J6.78, J6.79, J6.80
- net PWR_CTRL_SW: now also J10.161, J10.163, J5.1, J5.2, J6.1, J6.2, J9.161, J9.163; no longer J10.1, J10.2, J5.161, J5.163, J6.161, J6.163, J9.1, J9.2
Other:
- board text added: "Backplane V2.1 1842"
- board text removed: "Backplane V2.1 4218"
